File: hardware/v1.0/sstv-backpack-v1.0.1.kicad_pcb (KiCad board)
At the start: 2 copper layers, 38.1 x 63.5 mm, 15 parts, among them J1 Conn_01x03_Pin, J2 Conn_01x02_Pin, Q1 2N3904, SW1 SW_Push, SW2 SLW-1276864-4A-D, U1 ESP32-CAM

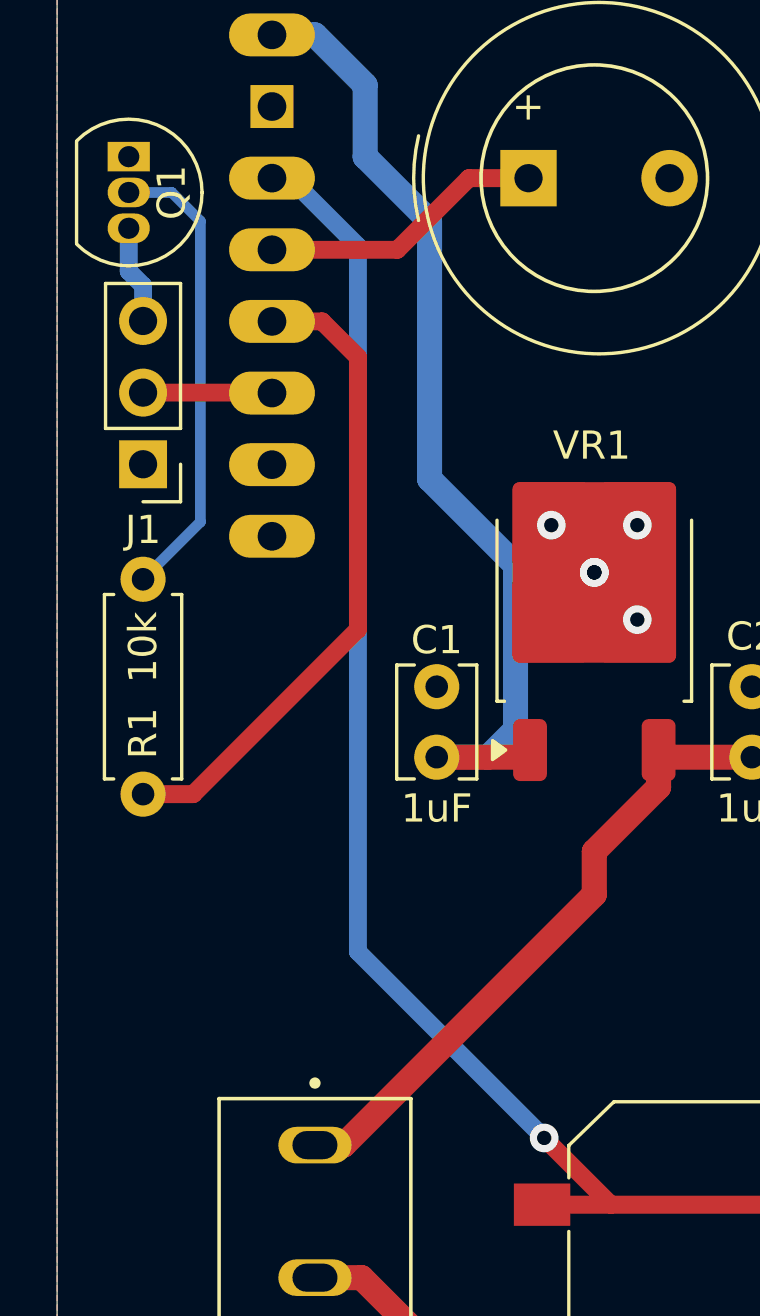
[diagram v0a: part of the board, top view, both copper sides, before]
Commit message: Update README and add pull-down resistors for PTT
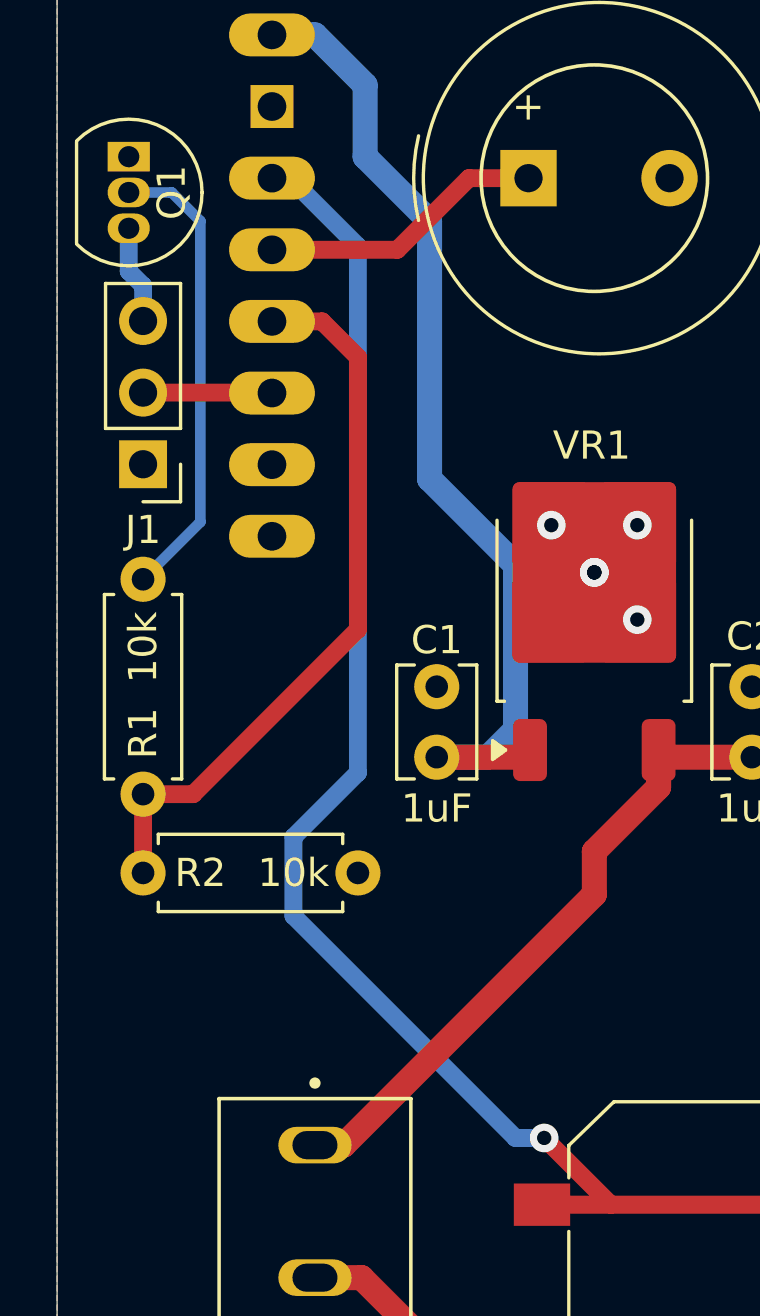
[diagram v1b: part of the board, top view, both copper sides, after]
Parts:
- added R2: 10k, Resistor_THT:R_Axial_DIN0207_L6.3mm_D2.5mm_P7.62mm_Horizontal, F.Cu at (150.4, 99.6)
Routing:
- net PTT_TRIG: track 23.3 -> 26.1 mm
- net /CAPTURE: track 56.1 -> 58.5 mm
